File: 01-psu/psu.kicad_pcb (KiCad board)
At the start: 2 copper layers, 250 x 32 mm, 38 parts, among them IC1 ISOLATED_DC-DC_CONV, J1 Barrel_Jack_Switch, J10 Conn_02x08_Odd_Even, J11 Conn_02x08_Odd_Even, J12 Conn_01x03, J13 Conn_01x03, J14 Conn_01x03, J2 Conn_02x08_Odd_Even, J3 Conn_02x08_Odd_Even, J4 Conn_02x08_Odd_Even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

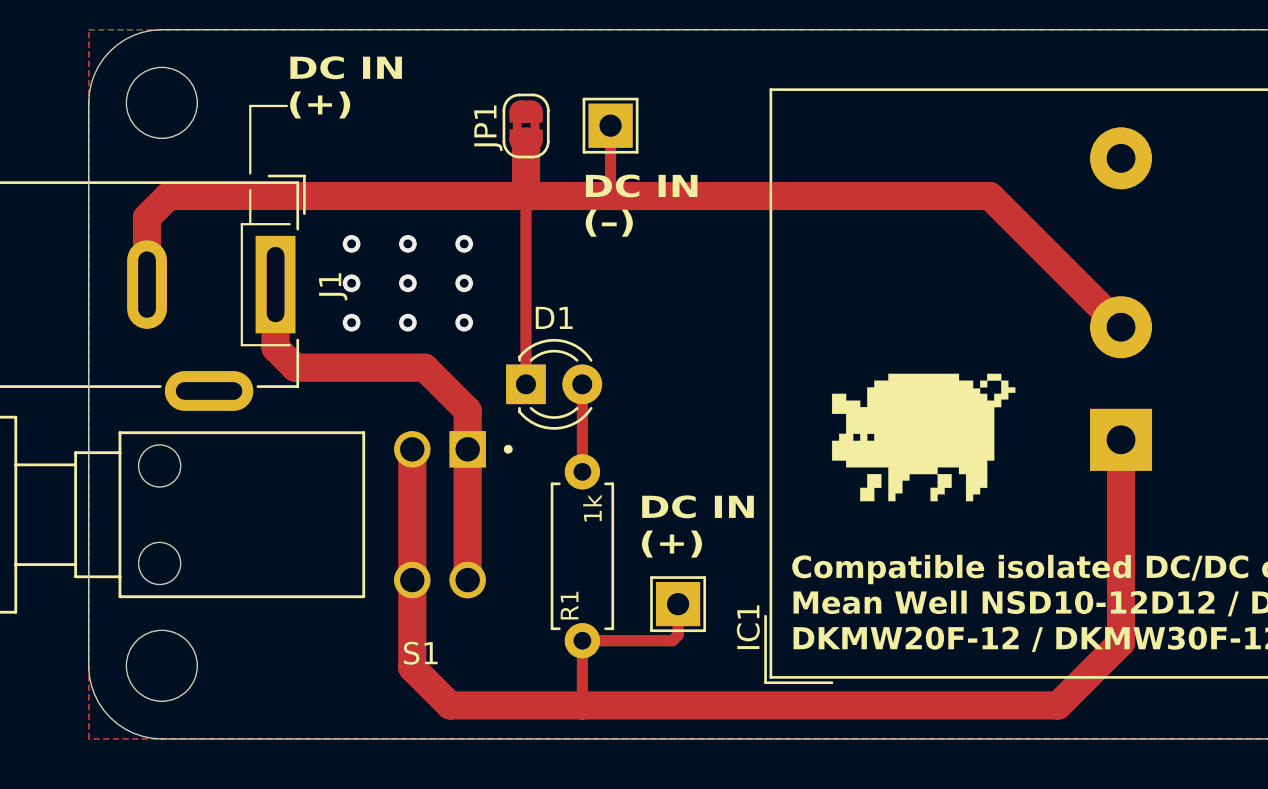
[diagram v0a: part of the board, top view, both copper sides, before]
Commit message: Added protection diode and terminal to PSU
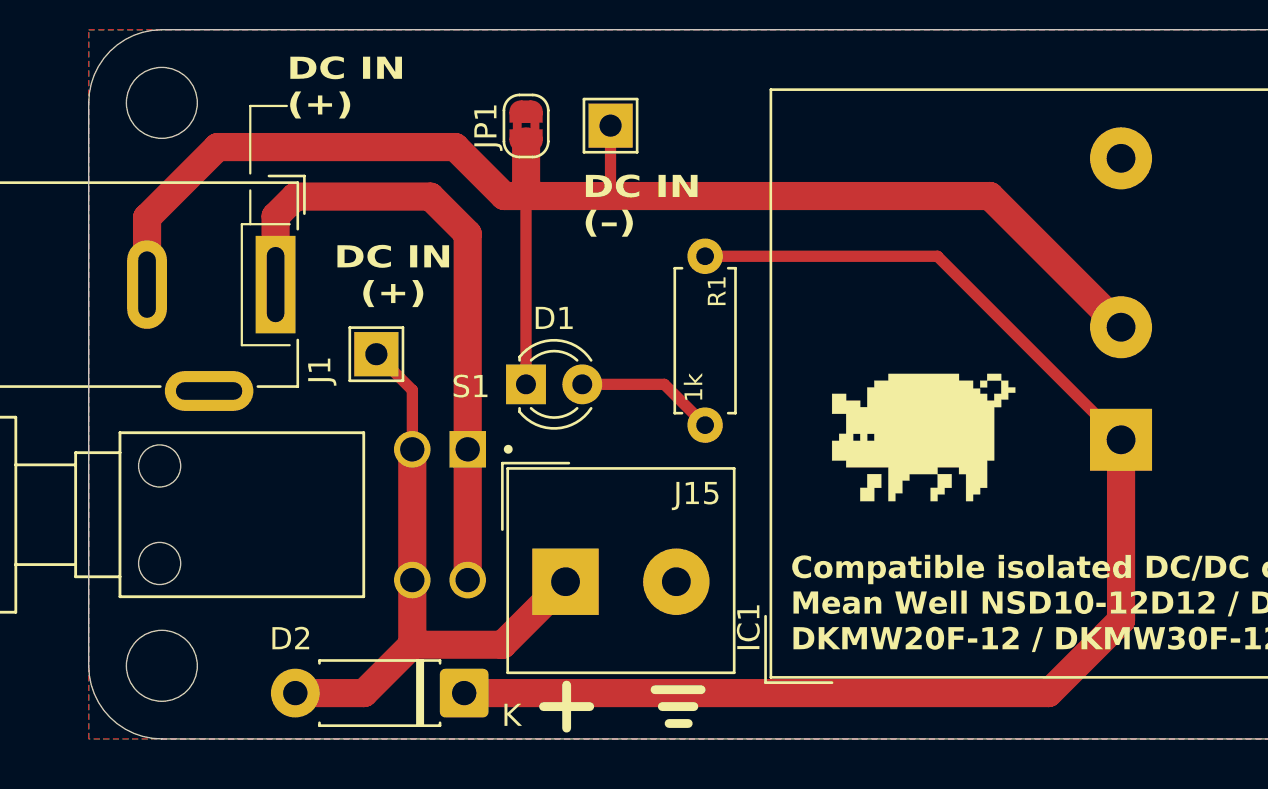
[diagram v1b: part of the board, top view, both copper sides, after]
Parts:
- added D2: 1N4001, Diode_THT:D_DO-41_SOD81_P7.62mm_Horizontal, F.Cu at (43.9, 109.9)
- added J15: Screw_Terminal_01x02, TerminalBlock_Altech:Altech_AK100_1x02_P5.00mm, F.Cu at (48.5, 104.9)
- moved R1 18.2 mm to (54.8, 90.2), turned to -90 degrees
- moved TP1 17.7 mm to (40.0, 94.6)
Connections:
- S1 pad 2: DC_IN_+ -> Net-(D2-A)
- S1 pad 4: DC_IN_+ -> Net-(D2-A)
- TP1 pad 1: DC_IN_+ -> Net-(D2-A)
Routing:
- net Net-(D2-A): track 0.00 -> 28.1 mm
- net Net-(J1-Pad1): track 20.3 -> 28.4 mm
- net Net-(D1-A): track 3.95 -> 6.31 mm
- net DC_IN_-: track 64.0 -> 65.8 mm
- net GND: vias 33 -> 24
